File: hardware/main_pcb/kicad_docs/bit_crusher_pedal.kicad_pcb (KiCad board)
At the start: 2 copper layers, 81.3 x 61 mm, 96 parts, among them J1 audio_input, J2 audio_output, J3 SWD_header, J4 9v_DC_in, J5 extern_resolution_CV, J6 extern_sample_rate_CV, J7 to_LED, Q1 MMBF5457, U1 MCP6002-xP, U2 MCP6002-xP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

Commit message: switch trimpot rotation
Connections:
- RV1 pad : GND -> (no net)
- RV2 pad : GND -> (no net)
- RV3 pad : GND -> (no net)
- RV4 pad 2: +9V -> Net-(R15-Pad1)
- RV5 pad 2: +9V -> Net-(R19-Pad1)
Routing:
- net +9V: track 130.1 -> 124.4 mm
- net Net-(R19-Pad1): track 5.08 -> 7.62 mm
- net Net-(R15-Pad1): track 5.08 -> 7.62 mm

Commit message: change gain pot to 100k
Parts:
- R5: value 22k -> 2k2
- R6: value 100k -> 10k
- RV1: value 1M -> 100k

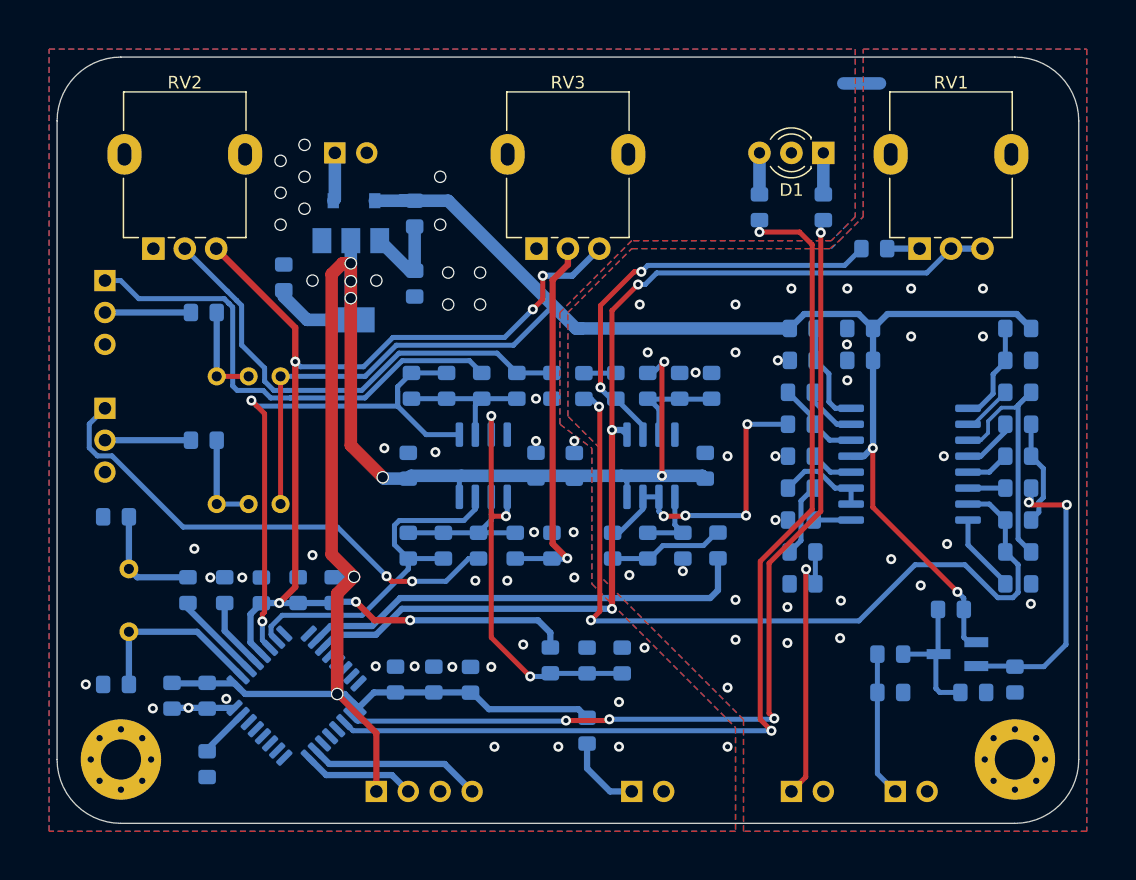
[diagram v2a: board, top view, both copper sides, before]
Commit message: rev 1.1, fix silkscreen, flip trimpots, adjust hpf
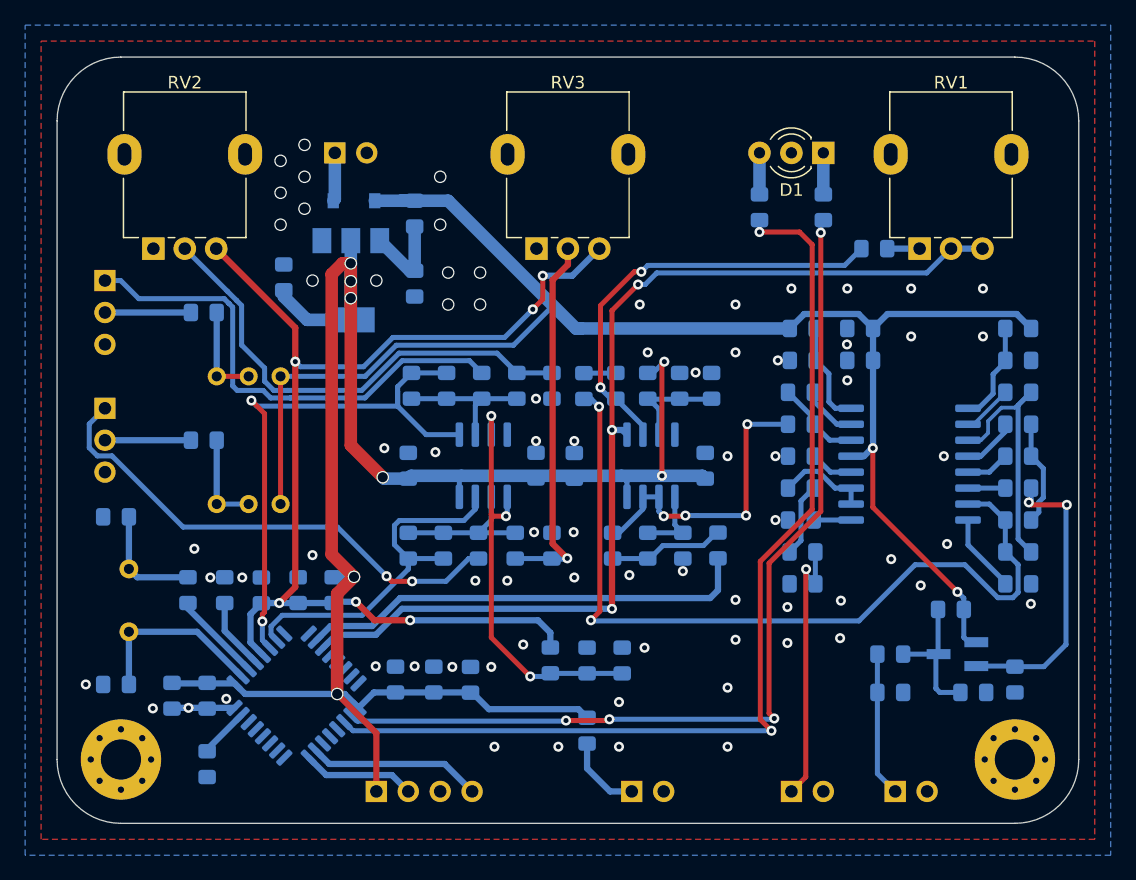
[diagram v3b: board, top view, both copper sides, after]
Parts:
- C4: value 47nF -> 220nF
- moved RV4 5.08 mm to (94.0, 76.2), turned to 0 degrees
- moved RV5 5.08 mm to (94.0, 86.4), turned to 0 degrees
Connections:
- RV4 pad 1: Net-(R15-Pad1) -> +9V
- RV4 pad 3: +9V -> Net-(R15-Pad1)
- RV5 pad 1: Net-(R19-Pad1) -> +9V
- RV5 pad 3: +9V -> Net-(R19-Pad1)
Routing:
- net GND: track 12.3 -> 9.37 mm
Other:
- board text added: "github.com/JordanAceto/bit_crusher_pedal rev 1.1 2020-11-8"
- board text removed: "github.com/JordanAceto/bit_crusher_pedal rev 1 2020-08-17"

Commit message: flip trimpots again, hopefully right this time
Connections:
- RV4 pad 1: +9V -> Net-(R15-Pad1)
- RV4 pad 3: Net-(R15-Pad1) -> +9V
- RV5 pad 1: +9V -> Net-(R19-Pad1)
- RV5 pad 3: Net-(R19-Pad1) -> +9V
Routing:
- net +9V: track 124.4 -> 132.0 mm, vias 2 -> 3
- net Net-(J5-Pad1): track 39.1 -> 37.9 mm
- net +3.3VA: track 90.8 -> 89.7 mm
- net Net-(R15-Pad1): track 7.62 -> 8.67 mm
- net Net-(R19-Pad1): track 7.62 -> 8.67 mm
